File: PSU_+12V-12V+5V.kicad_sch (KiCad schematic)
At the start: 61 parts, among them J1 PSU12a, J2 PSU12b, J3 PSU5, J4 230V, Q1 BC557, Q2 BC557, Q3 BC547, Q4 BC547, U1 LM317L, U2 LM317L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

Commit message: Put some nets
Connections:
- net CAPMULP: now reaches C7.1, Q3.2 (B), R7.2, R9.2
- net UNR12P: now reaches C9.1, D3.2 (A), D5.1 (K), Q1.1 (C), Q3.3 (E), U1.3 (VI)
- net IN12P: now reaches C3.1, D1.1 (+), D3.1 (K), Q1.3 (E), R3.1, R7.1
- net ADJ12N: now reaches C12.1, D8.2 (A), R13.1, R14.2, U2.1 (ADJ)
- net ADJ5V: now reaches C15.1, D11.2 (A), R10.1, R16.2, U3.1 (ADJ)
- net ADJ12P: now reaches C11.1, D7.2 (A), R11.1, R12.2, U1.1 (ADJ)
- net INP5V: now reaches C8.1, D10.1 (K), D9.1 (+), U3.3 (VI)
- net IN12N: now reaches C4.1, D2.1 (+), D4.1 (K), Q2.3 (E), R4.1, R5.1
- net UNR12N: now reaches C10.1, D4.2 (A), D6.1 (K), Q2.1 (C), Q4.3 (E), U2.3 (VI)
- net CAPMULN: now reaches C5.1, Q4.2 (B), R4.2, R6.2
- net 12Va renamed OUT12P
- net 12Vb renamed OUT12N
- net 5Vc renamed OUT5V
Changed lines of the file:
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@@
     (stroke (width 0) (type default) (color 0 0 0 0))
+  )
+  (label "ADJ12N" (at 93.98 113.665 90)
+    (effects (font (size 1.27 1.27)) (justify left bottom))
+  )
+  (label "CAPMULN" (at 68.58 114.935 0)
+    (effects (font (size 1.27 1.27)) (justify left bottom))
   )
   (label "NULL" (at 20.955 86.995 0)
     (effects (font (size 1.27 1.27)) (justify left bottom))
   )
+  (label "INP5V" (at 162.56 55.88 0)
+    (effects (font (size 1.27 1.27)) (justify left bottom))
+  )
   (label "MainP" (at 120.65 71.12 0)
+    (effects (font (size 1.27 1.27)) (justify left bottom))
+  )
+  (label "UNR12P" (at 82.55 27.305 90)
     (effects (font (size 1.27 1.27)) (justify left bottom))
   )
@@
     (effects (font (size 1.27 1.27)) (justify left bottom))
   )
+  (label "CAPMULP" (at 68.58 45.085 0)
+    (effects (font (size 1.27 1.27)) (justify left bottom))
+  )
+  (label "OUT5V" (at 201.295 55.88 0)
+    (effects (font (size 1.27 1.27)) (justify left bottom))
+  )
   (label "PHASE" (at 20.32 76.835 0)
     (effects (font (size 1.27 1.27)) (justify left bottom))
@@
     (effects (font (size 1.27 1.27)) (justify left bottom))
   )
-  (label "12Va" (at 104.775 27.305 0)
+  (label "ADJ12P" (at 93.98 43.18 90)
     (effects (font (size 1.27 1.27)) (justify left bottom))
   )
-  (label "12Vb" (at 106.045 97.155 0)
+  (label "IN12P" (at 49.53 27.305 0)
     (effects (font (size 1.27 1.27)) (justify left bottom))
   )
-  (label "5Vc" (at 193.04 55.88 0)
+  (label "ADJ5V" (at 180.975 71.12 90)
+    (effects (font (size 1.27 1.27)) (justify left bottom))
+  )
+  (label "OUT12N" (at 106.045 97.155 0)
     (effects (font (size 1.27 1.27)) (justify left bottom))
   )
@@
     (effects (font (size 1.27 1.27)) (justify left bottom))
   )
+  (label "UNR12N" (at 82.55 97.155 90)
+    (effects (font (size 1.27 1.27)) (justify left bottom))
+  )
+  (label "OUT12P" (at 106.045 27.305 0)
+    (effects (font (size 1.27 1.27)) (justify left bottom))
+  )
+  (label "IN12N" (at 46.355 97.155 0)
+    (effects (font (size 1.27 1.27)) (justify left bottom))
+  )

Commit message: Changed some values
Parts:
- C13, C14: value 1µ -> 10µ
- R12, R14: value 33k -> 1k8
- R15: value 100 -> 330
- R16: value 560 -> 330
- R6, R9: value 39k -> 100k
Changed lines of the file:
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@@
     (stroke (width 0) (type default) (color 0 0 0 0))
   )
-  (wire (pts (xy 20.32 86.995) (xy 24.765 86.995))
+  (wire (pts (xy 19.05 86.995) (xy 24.765 86.995))
     (stroke (width 0) (type default) (color 0 0 0 0))
   )
@@
     (stroke (width 0) (type default) (color 0 0 0 0))
   )
-  (wire (pts (xy 20.32 76.835) (xy 24.765 76.835))
+  (wire (pts (xy 18.415 76.835) (xy 24.765 76.835))
     (stroke (width 0) (type default) (color 0 0 0 0))
   )
@@
     (effects (font (size 1.27 1.27)) (justify left bottom))
   )
-  (label "NULL" (at 20.955 86.995 0)
+  (label "NULL" (at 19.05 86.995 0)
     (effects (font (size 1.27 1.27)) (justify left bottom))
   )
@@
     (effects (font (size 1.27 1.27)) (justify left bottom))
   )
-  (label "PHASE" (at 20.32 76.835 0)
-    (effects (font (size 1.27 1.27)) (justify left bottom))
-  )
-  (label "NULL" (at 133.985 88.9 0)
+  (label "PHASE" (at 18.415 76.835 0)
+    (effects (font (size 1.27 1.27)) (justify left bottom))
+  )
+  (label "NULL" (at 130.81 88.9 0)
     (effects (font (size 1.27 1.27)) (justify left bottom))
   )
@@
     (effects (font (size 1.27 1.27)) (justify left bottom))
   )
-  (label "PHASE" (at 133.35 78.74 0)
+  (label "PHASE" (at 130.175 78.74 0)
     (effects (font (size 1.27 1.27)) (justify left bottom))
   )
@@
       (effects (font (size 1.27 1.27)) (justify left))
     )
-    (property "Value" "1µ" (id 1) (at 107.315 46.99 0)
+    (property "Value" "10µ" (id 1) (at 107.315 46.99 0)
       (effects (font (size 1.27 1.27)) (justify left))
     )
@@
       (effects (font (size 1.27 1.27)) (justify right))
     )
-    (property "Value" "33k" (id 1) (at 99.06 125.73 0)
+    (property "Value" "1k8" (id 1) (at 99.06 125.73 0)
       (effects (font (size 1.27 1.27)) (justify right))
     )
@@
       (effects (font (size 1.27 1.27)) (justify left))
     )
-    (property "Value" "1µ" (id 1) (at 107.315 116.84 0)
+    (property "Value" "10µ" (id 1) (at 107.315 116.84 0)
       (effects (font (size 1.27 1.27)) (justify left))
     )
@@
   )
   (symbol (lib_id "Transformer:TEZ1.5-D-1") (at 141.605 83.82 0) (unit 1)
-    (in_bom yes) (on_board yes) (fields_autoplaced)
-    (property "Reference" "TR2" (id 0) (at 141.6431 73.66 0))
-    (property "Value" "Gerth_304.06" (id 1) (at 141.6431 76.2 0))
+    (in_bom yes) (on_board yes)
+    (property "Reference" "TR2" (id 0) (at 141.605 72.39 0))
+    (property "Value" "Gerth_304.06" (id 1) (at 141.605 74.93 0))
     (property "Footprint" "MyFootPrints:304.06_1.8VA" (id 2) (at 141.605 92.71 0)
       (effects (font (size 1.27 1.27) italic) hide)
@@
       (effects (font (size 1.27 1.27)) (justify right))
     )
-    (property "Value" "39k" (id 1) (at 72.39 126.365 0)
+    (property "Value" "100k" (id 1) (at 72.39 126.365 0)
       (effects (font (size 1.27 1.27)) (justify right))
     )
@@
       (effects (font (size 1.27 1.27)) (justify right))
     )
-    (property "Value" "560" (id 1) (at 191.77 79.375 0)
+    (property "Value" "330" (id 1) (at 191.77 79.375 0)
       (effects (font (size 1.27 1.27)) (justify right))
     )
@@
       (effects (font (size 1.27 1.27)) (justify right))
     )
-    (property "Value" "100" (id 1) (at 191.135 86.995 0)
+    (property "Value" "330" (id 1) (at 191.135 86.995 0)
       (effects (font (size 1.27 1.27)) (justify right))
     )
@@
       (effects (font (size 1.27 1.27)) (justify right))
     )
-    (property "Value" "39k" (id 1) (at 72.39 57.15 0)
+    (property "Value" "100k" (id 1) (at 72.39 57.15 0)
       (effects (font (size 1.27 1.27)) (justify right))
     )
@@
       (effects (font (size 1.27 1.27)) (justify right))
     )
-    (property "Value" "33k" (id 1) (at 99.06 55.88 0)
+    (property "Value" "1k8" (id 1) (at 99.06 55.88 0)
       (effects (font (size 1.27 1.27)) (justify right))
     )
@@
     )
     (path "/01ff2b47-b878-42f0-ab8c-28aed1749844"
-      (reference "C13") (unit 1) (value "1µ") (footprint "Capacitor_THT:CP_Radial_D5.0mm_P2.50mm")
+      (reference "C13") (unit 1) (value "10µ") (footprint "Capacitor_THT:CP_Radial_D5.0mm_P2.50mm")
     )
     (path "/489cab34-4cb3-4d8e-884c-b72b7a5335fa"
-      (reference "C14") (unit 1) (value "1µ") (footprint "Capacitor_THT:CP_Radial_D5.0mm_P2.50mm")
+      (reference "C14") (unit 1) (value "10µ") (footprint "Capacitor_THT:CP_Radial_D5.0mm_P2.50mm")
     )
     (path "/219786c6-d67d-43e1-bfdf-7b0e7a9bf9e2"
@@
     )
     (path "/7763febc-24be-40eb-bf4a-ad60f8b28a67"
-      (reference "R6") (unit 1) (value "39k") (footprint "Resistor_SMD:R_1206_3216Metric_Pad1.30x1.75mm_HandSolder")
+      (reference "R6") (unit 1) (value "100k") (footprint "Resistor_SMD:R_1206_3216Metric_Pad1.30x1.75mm_HandSolder")
     )
     (path "/4a1bd396-4c5d-468d-b5d4-07f5632a4864"
@@
     )
     (path "/ca774817-3564-4174-9734-86fddd567a63"
-      (reference "R9") (unit 1) (value "39k") (footprint "Resistor_SMD:R_1206_3216Metric_Pad1.30x1.75mm_HandSolder")
+      (reference "R9") (unit 1) (value "100k") (footprint "Resistor_SMD:R_1206_3216Metric_Pad1.30x1.75mm_HandSolder")
     )
     (path "/aa374c84-ef44-4abc-888a-d78211372fe5"
@@
     )
     (path "/e7d4355e-0b6a-4898-9c1b-b93beb5626c4"
-      (reference "R12") (unit 1) (value "33k") (footprint "Resistor_SMD:R_1206_3216Metric_Pad1.30x1.75mm_HandSolder")
+      (reference "R12") (unit 1) (value "1k8") (footprint "Resistor_SMD:R_1206_3216Metric_Pad1.30x1.75mm_HandSolder")
     )
     (path "/303be9cb-f48d-4841-a61e-69f0f4537588"
@@
     )
     (path "/3c6f602a-4e95-4cff-a56a-f4ce11b9656f"
-      (reference "R14") (unit 1) (value "33k") (footprint "Resistor_SMD:R_1206_3216Metric_Pad1.30x1.75mm_HandSolder")
+      (reference "R14") (unit 1) (value "1k8") (footprint "Resistor_SMD:R_1206_3216Metric_Pad1.30x1.75mm_HandSolder")
     )
     (path "/bdc0d6a1-83d8-4c7c-a5c3-15e6995d801d"
-      (reference "R15") (unit 1) (value "100") (footprint "Resistor_SMD:R_1206_3216Metric_Pad1.30x1.75mm_HandSolder")
+      (reference "R15") (unit 1) (value "330") (footprint "Resistor_SMD:R_1206_3216Metric_Pad1.30x1.75mm_HandSolder")
     )
     (path "/bbfde6a8-1c48-4bd7-b70d-43b8ba21483e"
-      (reference "R16") (unit 1) (value "560") (footprint "Resistor_SMD:R_1206_3216Metric_Pad1.30x1.75mm_HandSolder")
+      (reference "R16") (unit 1) (value "330") (footprint "Resistor_SMD:R_1206_3216Metric_Pad1.30x1.75mm_HandSolder")
     )
     (path "/baa1157e-dd71-4256-a2a5-b85c05faee87"

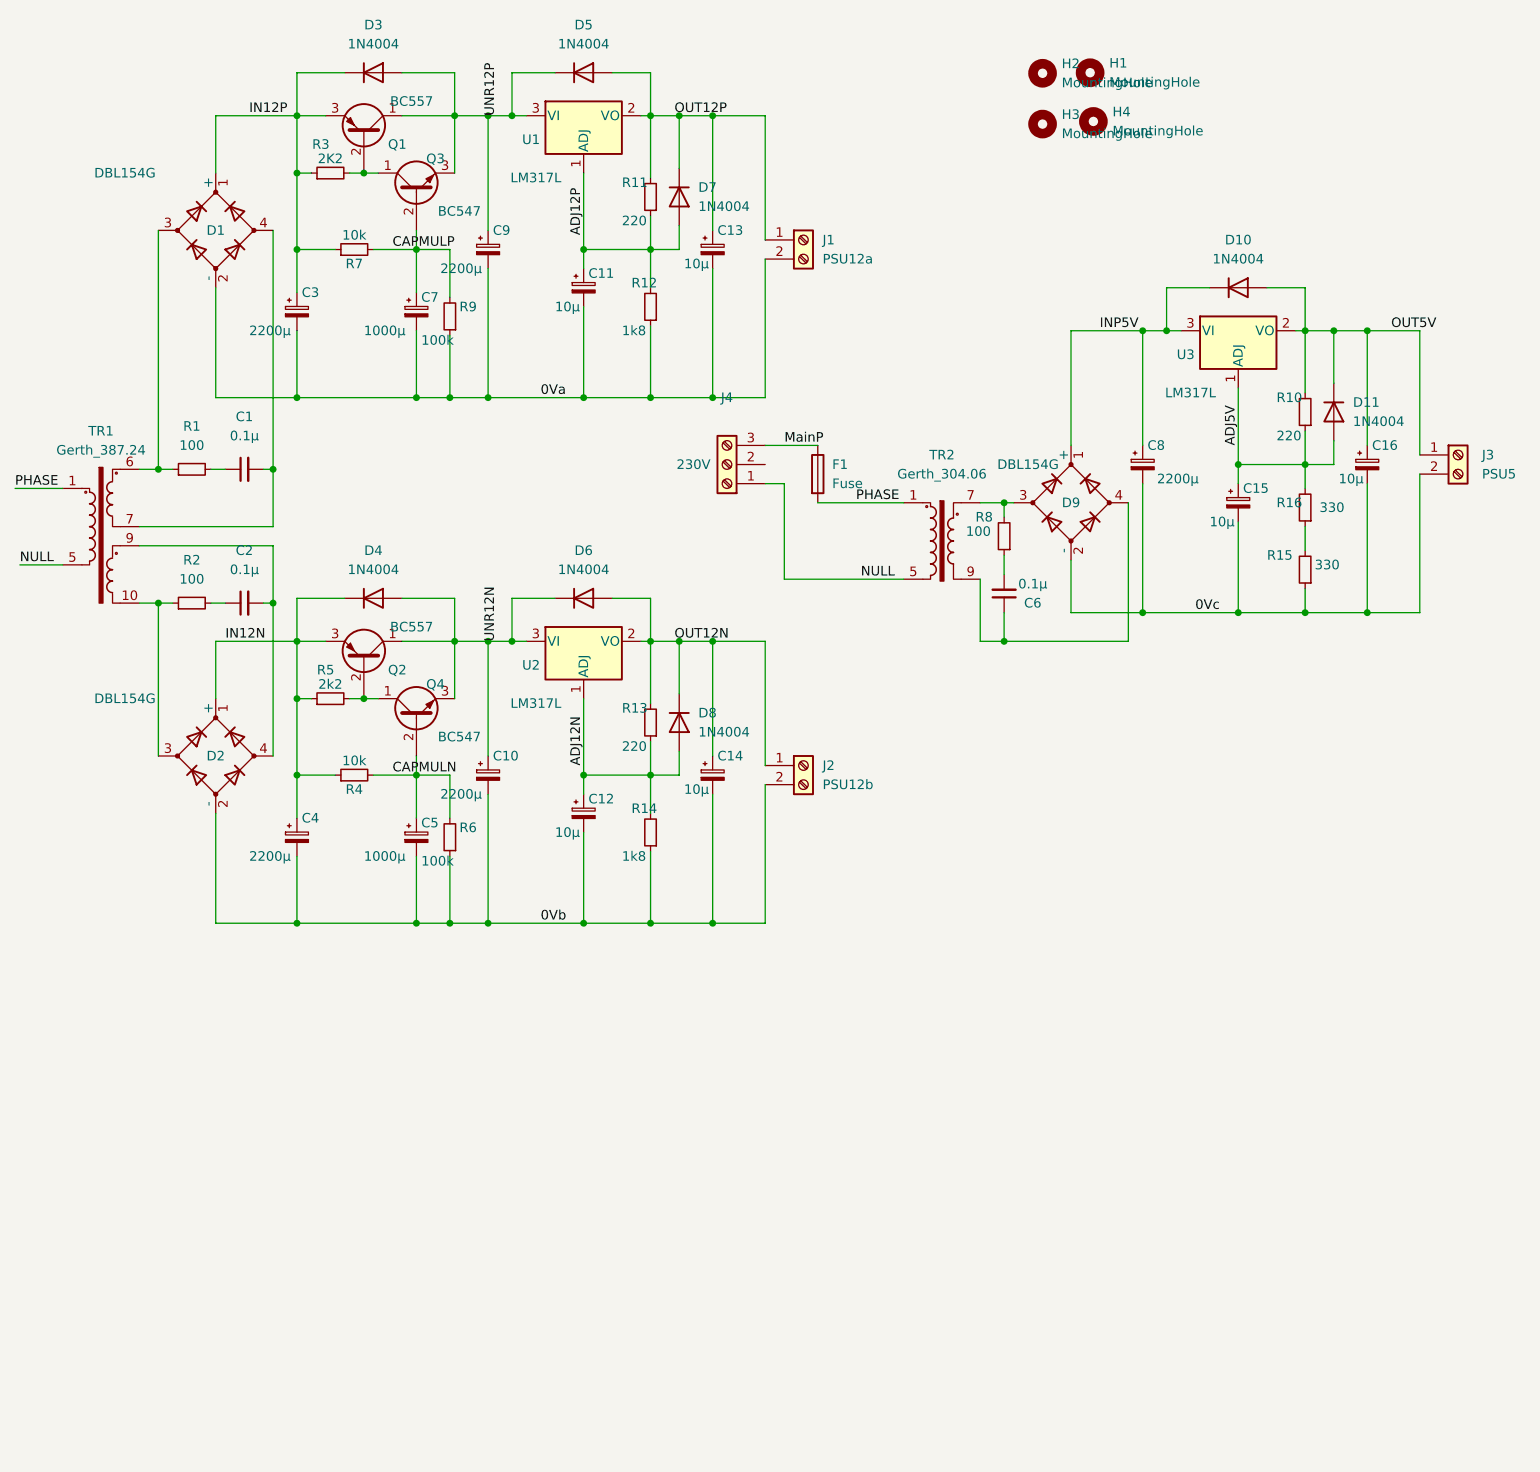
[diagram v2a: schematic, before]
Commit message: Change page setup for printing on A4
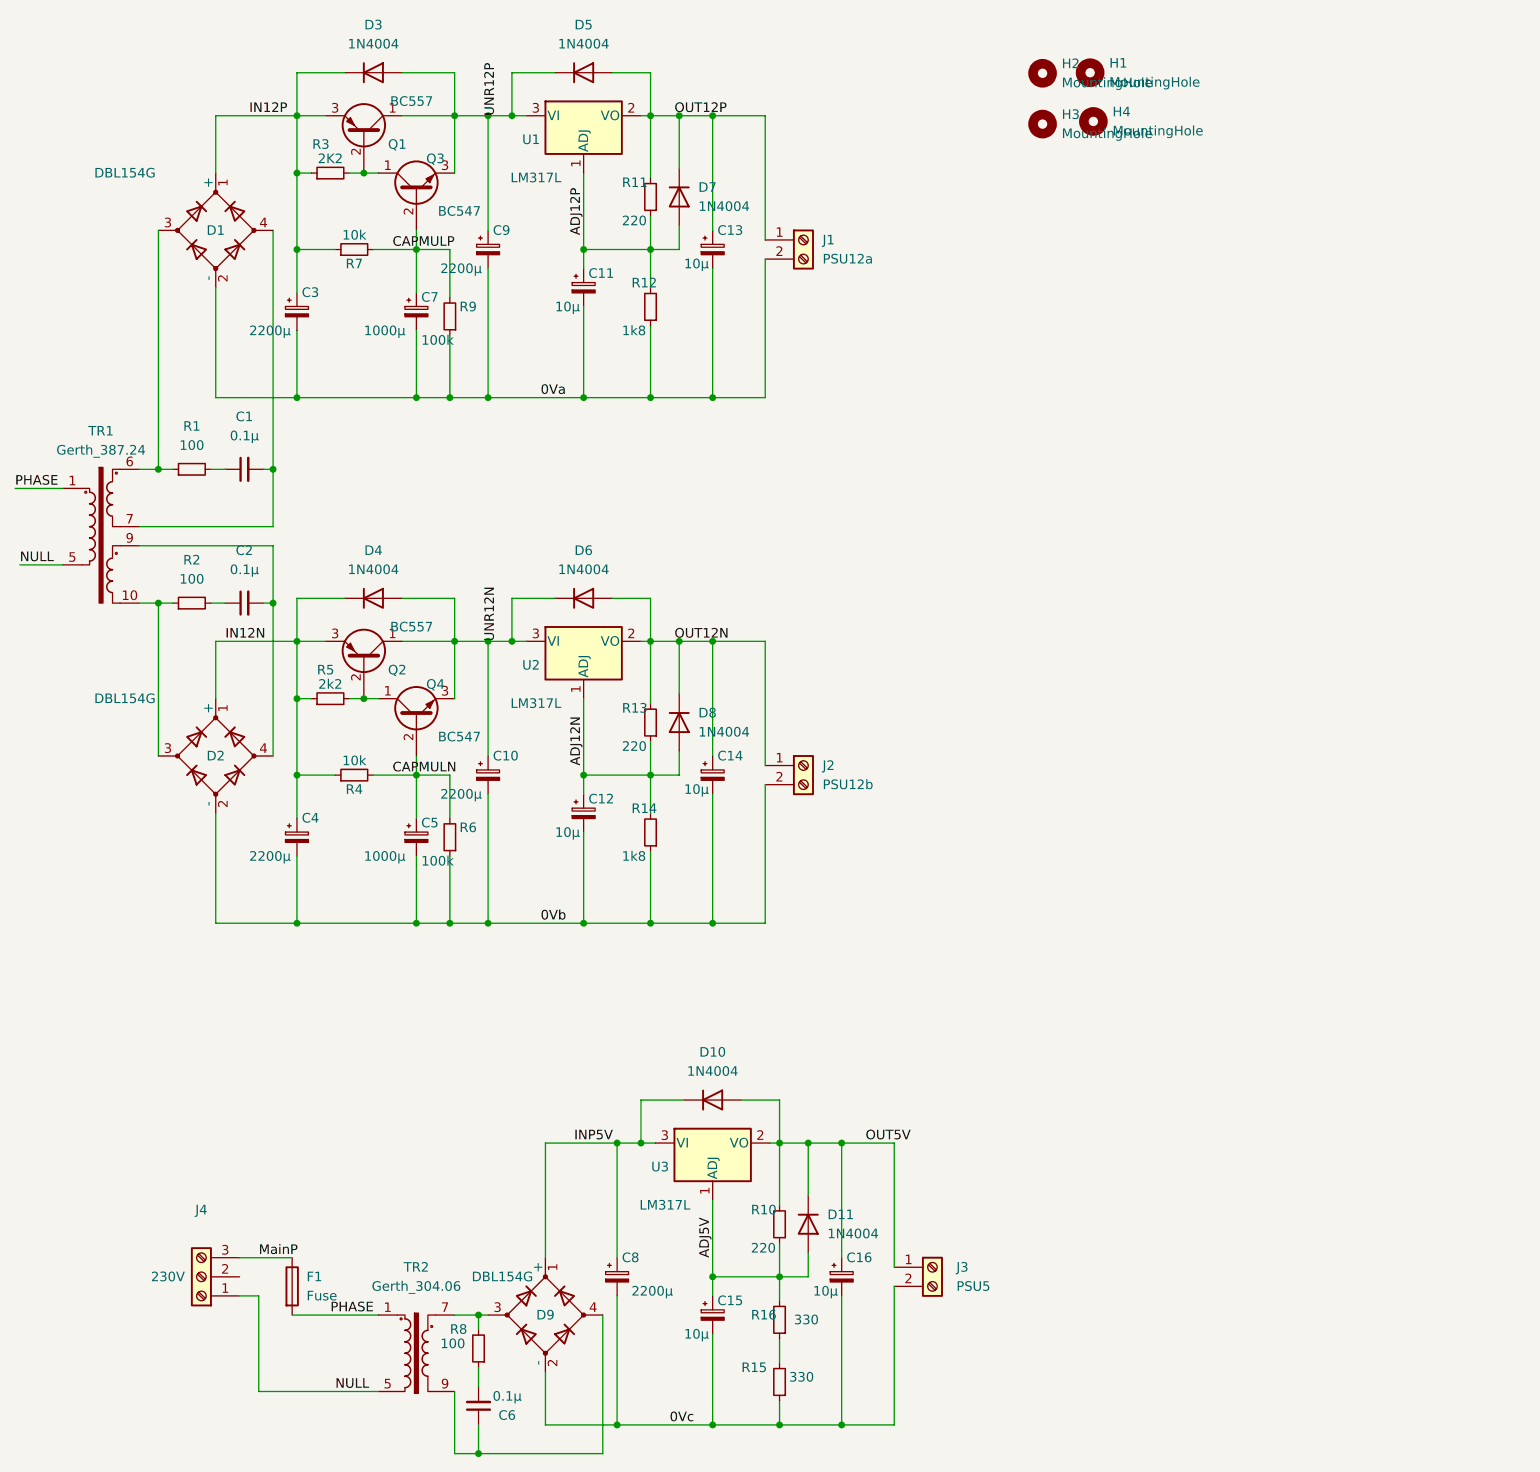
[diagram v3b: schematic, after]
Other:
- moved on the sheet: C15, C16, C6, C8, D10, D11, D9, F1, J3, J4, R10, R15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
